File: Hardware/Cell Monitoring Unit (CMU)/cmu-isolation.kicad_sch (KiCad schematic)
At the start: 26 parts, among them T1 CEP99-102, T2 CEP99-102, U1 PESD5V0L2BT, U2 PESD5V0L2BT

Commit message: A bit more schematic polishing
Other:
- note added: "Middle module: use both COMH and COML. End module: use one side and terminate the unused side. Ring: use both sides and terminate chain ends."
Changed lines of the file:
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@@
+		)
+	)
+	(text "Middle module: use both COMH and COML.\nEnd module: use one side and terminate the unused side.\nRing: use both sides and terminate chain ends."
+		(exclude_from_sim no)
+		(at 191.008 142.748 0)
+		(effects
+			(font
+				(size 1.27 1.27)
+				(thickness 0.1588)
+			)
+			(justify left)
 		)
 	)

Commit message: updated cmu layout
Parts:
- renumbered C38 to C52, C39 to C53, C29 to C54, C40 to C55, C47 to C56, C19 to C57, R41 to R47, R42 to R48, R43 to R49, R44 to R50, R31 to R51, R32 to R52, R45 to R53, R46 to R54, R48 to R55, R49 to R56, R22 to R57, R21 to R58, R10 to R59, R11 to R60, R53 to R61, R54 to R62, T2 to T1, T1 to T2, U1 to U3, U2 to U4
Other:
- note added: "Isolated Daisy-Chain COM Interface"
- note added: "Middle CMU: connect both COMH and COML sides. End CMU: use one COM side and terminate the unused side. Ring topology: use both COM sides and terminate only the chain ends."
- note removed: "Middle module: use both COMH and COML. End module: use one side and terminate the unused side. Ring: use both sides and terminate chain ends."
- note removed: "Tranformer Isolation For COM Communication"
- moved on the sheet: C52, C53, C54, C55, C56, C57, R47, R48, R49, R50, R51, R52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

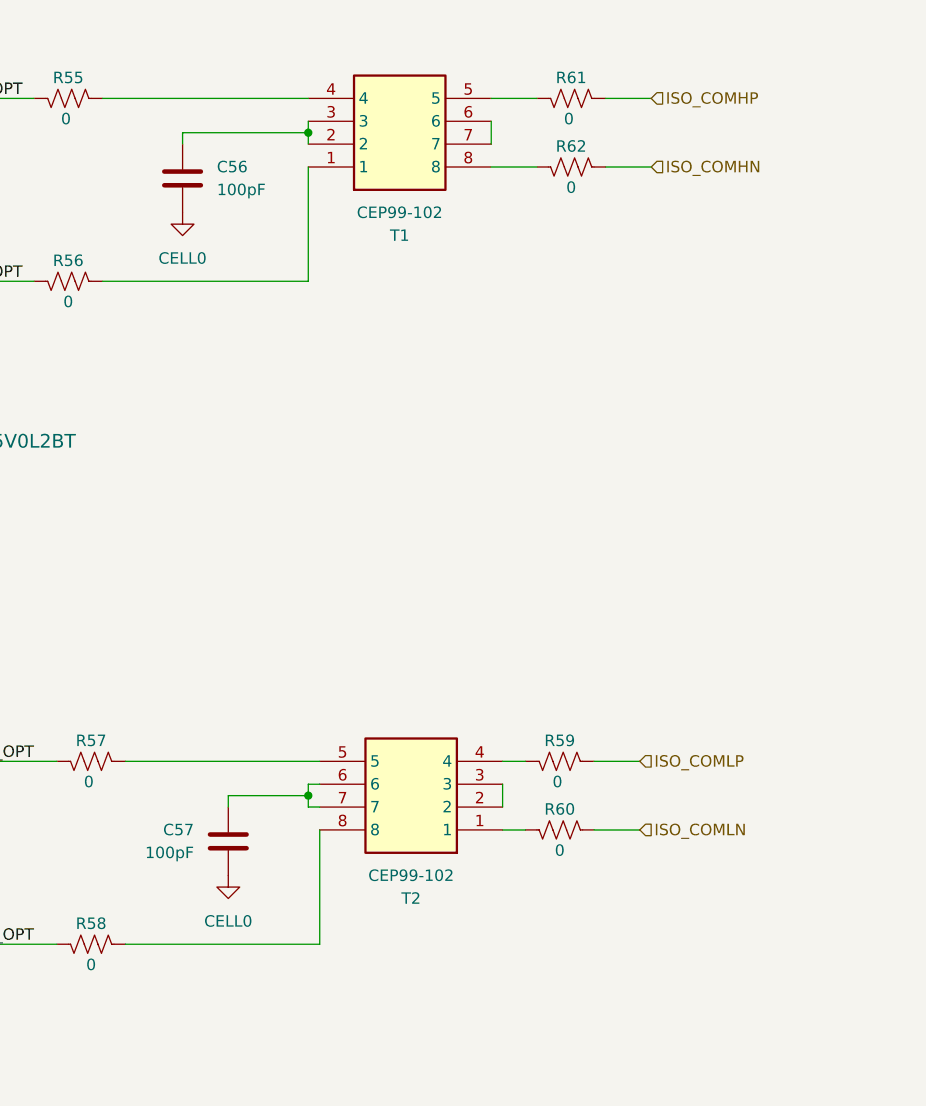
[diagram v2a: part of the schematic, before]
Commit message: change iso+update cmu BOM
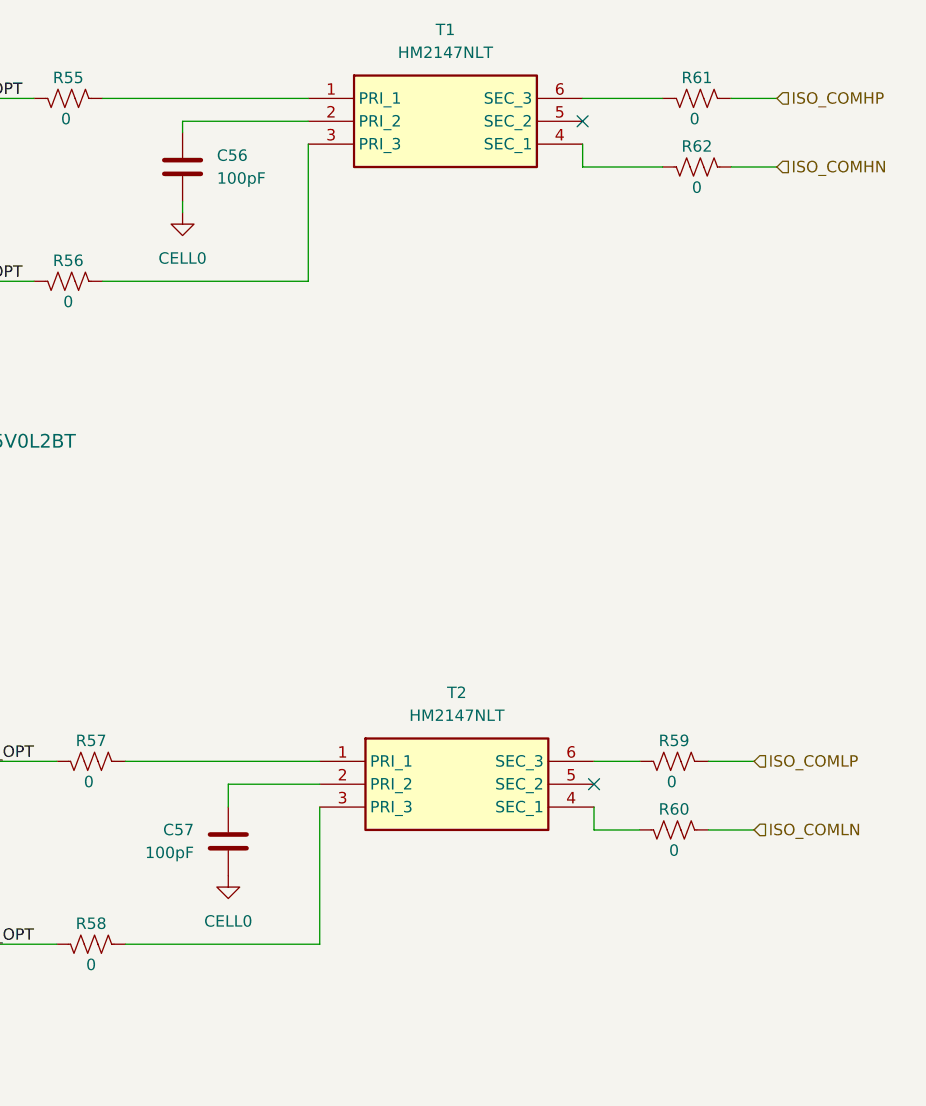
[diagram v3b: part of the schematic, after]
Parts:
- removed T1, T2: CEP99-102, Footprints:CEP99102, symbol CEP99-102:CEP99-102
- added T1, T2: HM2147NLT, Footprints:HM2147NLT, symbol HM2147NLT:HM2147NLT
- C52, C53, C54, C55, C56, C57: DIS (none) -> DigiKey; DPN (none) -> 311-4295-1-ND; MFR (none) -> YAGEO; MPN (none) -> CC0805KRNPO9BN101; Purchase Link (none) -> https://www.digikey.com/en/products/detail/yageo/CC0805KRNP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
- R47, R48, R49, R50: DIS (none) -> DigiKey; DPN (none) -> 311-499CRCT-ND; MFR (none) -> YAGEO; MPN (none) -> RC0805FR-07499RL; Purchase Link (none) -> https://www.digikey.com/en/products/detail/yageo/RC0805FR-0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
- R51, R52, R53, R54: DIS (none) -> DigiKey; DPN (none) -> 311-51.0CRCT-ND; MFR (none) -> YAGEO; MPN (none) -> RC0805FR-0751RL; Purchase Link (none) -> https://www.digikey.com/en/products/detail/yageo/RC0805FR-0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
- R55, R56, R57, R58, R59, R60, R61, R62: DIS (none) -> DigiKey; DPN (none) -> 311-0.0ARCT-ND; MFR (none) -> YAGEO; MPN (none) -> RC0805JR-070RL; Purchase Link (none) -> https://www.digikey.com/en/products/detail/yageo/RC0805JR-0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
- U3, U4: DIS (none) -> DigiKey; DPN (none) -> 1727-3834-1-ND; MFR (none) -> Nexperia; MPN (none) -> PESD5V0L2BT,215; Purchase Link (none) -> https://www.digikey.com/en/products/detail/nexperia-usa-inc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
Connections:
- net at R55.1: now also T1.1 (PRI_1)
- net at R60.2: now also T2.4 (SEC_1)
- net at R59.2: now also T2.6 (SEC_3)
- net at R57.1: now also T2.1 (PRI_1)
- net at C57.1: now also T2.2 (PRI_2)
- net at R58.1: now also T2.3 (PRI_3)
- net at R56.1: now also T1.3 (PRI_3)
- net at C56.1: now also T1.2 (PRI_2)
- net at R62.2: now also T1.4 (SEC_1)
- net at R61.2: now also T1.6 (SEC_3)
- no-connect marks 0 -> 2
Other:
- moved on the sheet: C56, R59, R60, R61, R62
